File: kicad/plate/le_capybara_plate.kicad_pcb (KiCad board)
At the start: 2 copper layers, 231.6 x 92.5 mm, 66 parts, among them SW1 EC_SW, SW10 EC_SW, SW11 EC_SW, SW12 EC_SW, SW13 EC_SW, SW14 EC_SW, SW15 EC_SW, SW16 EC_SW, SW17 EC_SW, SW18 EC_SW, SW19 EC_SW, SW2 EC_SW, SW20 EC_SW, SW21 EC_SW, SW22 EC_SW, SW23 EC_SW, SW24 EC_SW, SW25 EC_SW, SW26 EC_SW, SW27 EC_SW, SW28 EC_SW, SW29 EC_SW, SW3 EC_SW, SW30 EC_SW, SW31 EC_SW, SW32 EC_SW, SW33 EC_SW, SW34 EC_SW, SW4 EC_SW, SW5 EC_SW, SW6 EC_SW, SW7 EC_SW, SW8 EC_SW, SW9 EC_SW

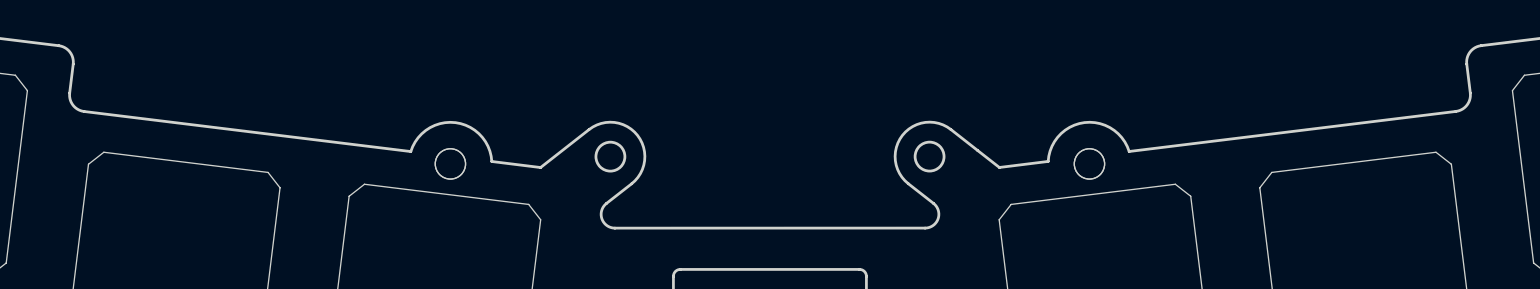
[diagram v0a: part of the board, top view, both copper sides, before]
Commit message: remove top mounting hole for chiffre+ compatibility
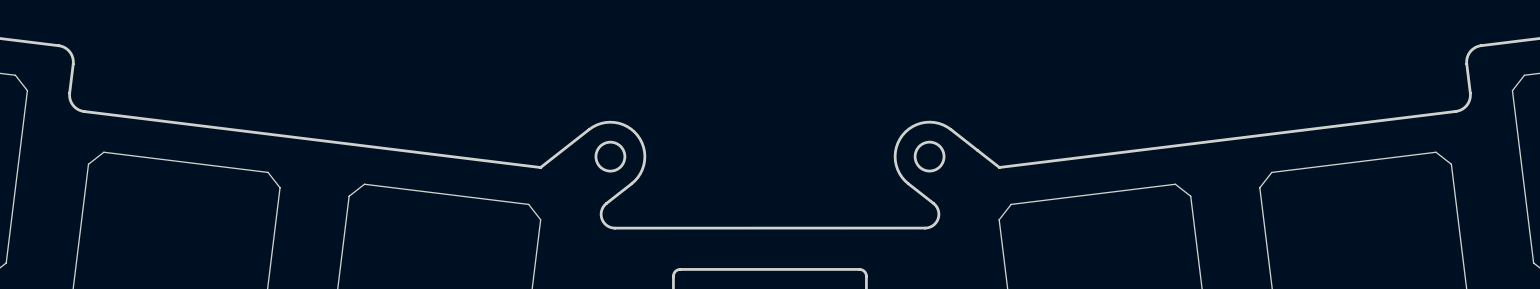
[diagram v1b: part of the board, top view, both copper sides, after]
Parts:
- removed H13, H5: M2 Hole, capacitive_sensors:MountingHole_2.2mm_M2
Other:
- outline, holes or cut-outs redrawn
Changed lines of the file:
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@@
-    (pad "" np_thru_hole circle (at 0 0) (size 2.2 2.2) (drill 2.2) (layers "*.Cu" "*.Mask"))
-  )
-  (footprint "capacitive_sensors:MountingHole_2.2mm_M2" (layer "F.Cu")
-    (at 123.459443 69.702874)
-    (descr "Mounting Hole 2.2mm, no annular, M2")
-    (tags "mounting hole 2.2mm no annular m2")
-    (property "Sheetfile" "le_capybara_plate.kicad_sch")
-    (property "Sheetname" "")
-    (property "ki_description" "Mounting Hole without connection")
-    (property "ki_keywords" "mounting hole")
-    (attr exclude_from_pos_files)
-    (fp_text reference "H13" (at 0 -3.2 unlocked) (layer "F.SilkS") hide
-        (effects (font (size 0.8 0.8) (thickness 0.15)))
-    )
-    (fp_text value "M2 Hole" (at 0 3.2) (layer "F.Fab")
-        (effects (font (size 1 1) (thickness 0.15)))
-    )
-    (fp_text user "${REFERENCE}" (at 0 0) (layer "F.Fab")
-        (effects (font (size 1 1) (thickness 0.15)))
-    )
-    (fp_circle (center 0 0) (end 1.5 0)
-      (stroke (width 0.1) (type default)) (fill none) (layer "Dwgs.User"))
-    (fp_circle (center 0 0) (end 1.1 0)
-      (stroke (width 0.05) (type solid)) (fill none) (layer "Edge.Cuts"))
-    (fp_circle (center 0 0) (end 1.5 0)
-      (stroke (width 0.05) (type solid)) (fill none) (layer "F.CrtYd"))
     (pad "" np_thru_hole circle (at 0 0) (size 2.2 2.2) (drill 2.2) (layers "*.Cu" "*.Mask"))
   )
@@
     (pad "" np_thru_hole circle (at 0 0 7) (size 2.2 2.2) (drill 2.2) (layers "*.Cu" "*.Mask"))
   )
-  (footprint "capacitive_sensors:MountingHole_2.2mm_M2" (layer "F.Cu")
-    (at 169.819499 69.702872)
-    (descr "Mounting Hole 2.2mm, no annular, M2")
-    (tags "mounting hole 2.2mm no annular m2")
-    (property "Sheetfile" "le_capybara_plate.kicad_sch")
-    (property "Sheetname" "")
-    (property "ki_description" "Mounting Hole without connection")
-    (property "ki_keywords" "mounting hole")
-    (attr exclude_from_pos_files)
-    (fp_text reference "H5" (at 0 -3.2 unlocked) (layer "F.SilkS") hide
-        (effects (font (size 0.8 0.8) (thickness 0.15)))
-    )
-    (fp_text value "M2 Hole" (at 0 3.2) (layer "F.Fab")
-        (effects (font (size 1 1) (thickness 0.15)))
-    )
-    (fp_text user "${REFERENCE}" (at 0 0) (layer "F.Fab")
-        (effects (font (size 1 1) (thickness 0.15)))
-    )
-    (fp_circle (center 0 0) (end 1.5 0)
-      (stroke (width 0.1) (type default)) (fill none) (layer "Dwgs.User"))
-    (fp_circle (center 0 0) (end 1.1 0)
-      (stroke (width 0.05) (type solid)) (fill none) (layer "Edge.Cuts"))
-    (fp_circle (center 0 0) (end 1.5 0)
-      (stroke (width 0.05) (type solid)) (fill none) (layer "F.CrtYd"))
-    (pad "" np_thru_hole circle (at 0 0) (size 2.2 2.2) (drill 2.2) (layers "*.Cu" "*.Mask"))
-  )
   (footprint "capacitive_sensors:plate_cut_1U_topre" (layer "F.Cu")
     (at 85.056867 69.785834 83)
@@
   (gr_circle (center 158.221506 69.172298) (end 159.271506 69.1723)
     (stroke (width 0.2) (type solid)) (fill none) (layer "Edge.Cuts"))
-  (gr_line (start 126.463206 69.527659) (end 130.002631 69.966074)
-    (stroke (width 0.2) (type default)) (layer "Edge.Cuts"))
   (gr_line (start 154.640692 94.348132) (end 154.640691 135.34813)
     (stroke (width 0.2) (type default)) (layer "Edge.Cuts"))
@@
   (gr_line (start 243.523049 64.389422) (end 250.916415 63.481631)
     (stroke (width 0.2) (type default)) (layer "Edge.Cuts"))
-  (gr_line (start 163.286305 69.962015) (end 166.82573 69.5236)
-    (stroke (width 0.2) (type default)) (layer "Edge.Cuts"))
   (gr_line (start 153.640692 136.348133) (end 139.640692 136.348133)
     (stroke (width 0.2) (type default)) (layer "Edge.Cuts"))
@@
     (stroke (width 0.2) (type default)) (layer "Edge.Cuts"))
   (gr_arc (start 126.21475 140.017014) (mid 126.547395 139.397299) (end 127.20579 139.149902)
-    (stroke (width 0.2) (type default)) (layer "Edge.Cuts"))
-  (gr_arc (start 120.587334 68.806191) (mid 123.827156 66.708266) (end 126.463206 69.527659)
     (stroke (width 0.2) (type default)) (layer "Edge.Cuts"))
   (gr_arc (start 236.693539 120.055111) (mid 236.898063 119.317571) (end 237.564216 118.940695)
@@
   (gr_arc (start 126.925555 147.603746) (mid 126.196244 151.063278) (end 122.736725 150.333896)
     (stroke (width 0.2) (type solid)) (layer "Edge.Cuts"))
-  (gr_line (start 96.884652 65.899696) (end 120.587334 68.806191)
-    (stroke (width 0.2) (type solid)) (layer "Edge.Cuts"))
-  (gr_line (start 172.701602 68.802132) (end 196.404284 65.895637)
+  (gr_line (start 96.884652 65.899696) (end 130.002631 69.966074)
+    (stroke (width 0.2) (type solid)) (layer "Edge.Cuts"))
+  (gr_line (start 163.286305 69.962015) (end 196.404284 65.895637)
     (stroke (width 0.2) (type solid)) (layer "Edge.Cuts"))
   (gr_arc (start 153.639472 90.858057) (mid 153.493025 91.21161) (end 153.139472 91.358057)
@@
   (gr_arc (start 172.728056 146.991461) (mid 173.036607 146.689003) (end 173.443954 146.544944)
     (stroke (width 0.2) (type default)) (layer "Edge.Cuts"))
-  (gr_arc (start 166.82573 69.5236) (mid 169.461802 66.704204) (end 172.701602 68.802132)
-    (stroke (width 0.2) (type default)) (layer "Edge.Cuts"))
   (gr_line (start 216.943315 60.036384) (end 217.200764 62.13314)
